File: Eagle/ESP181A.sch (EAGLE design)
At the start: 30 parts

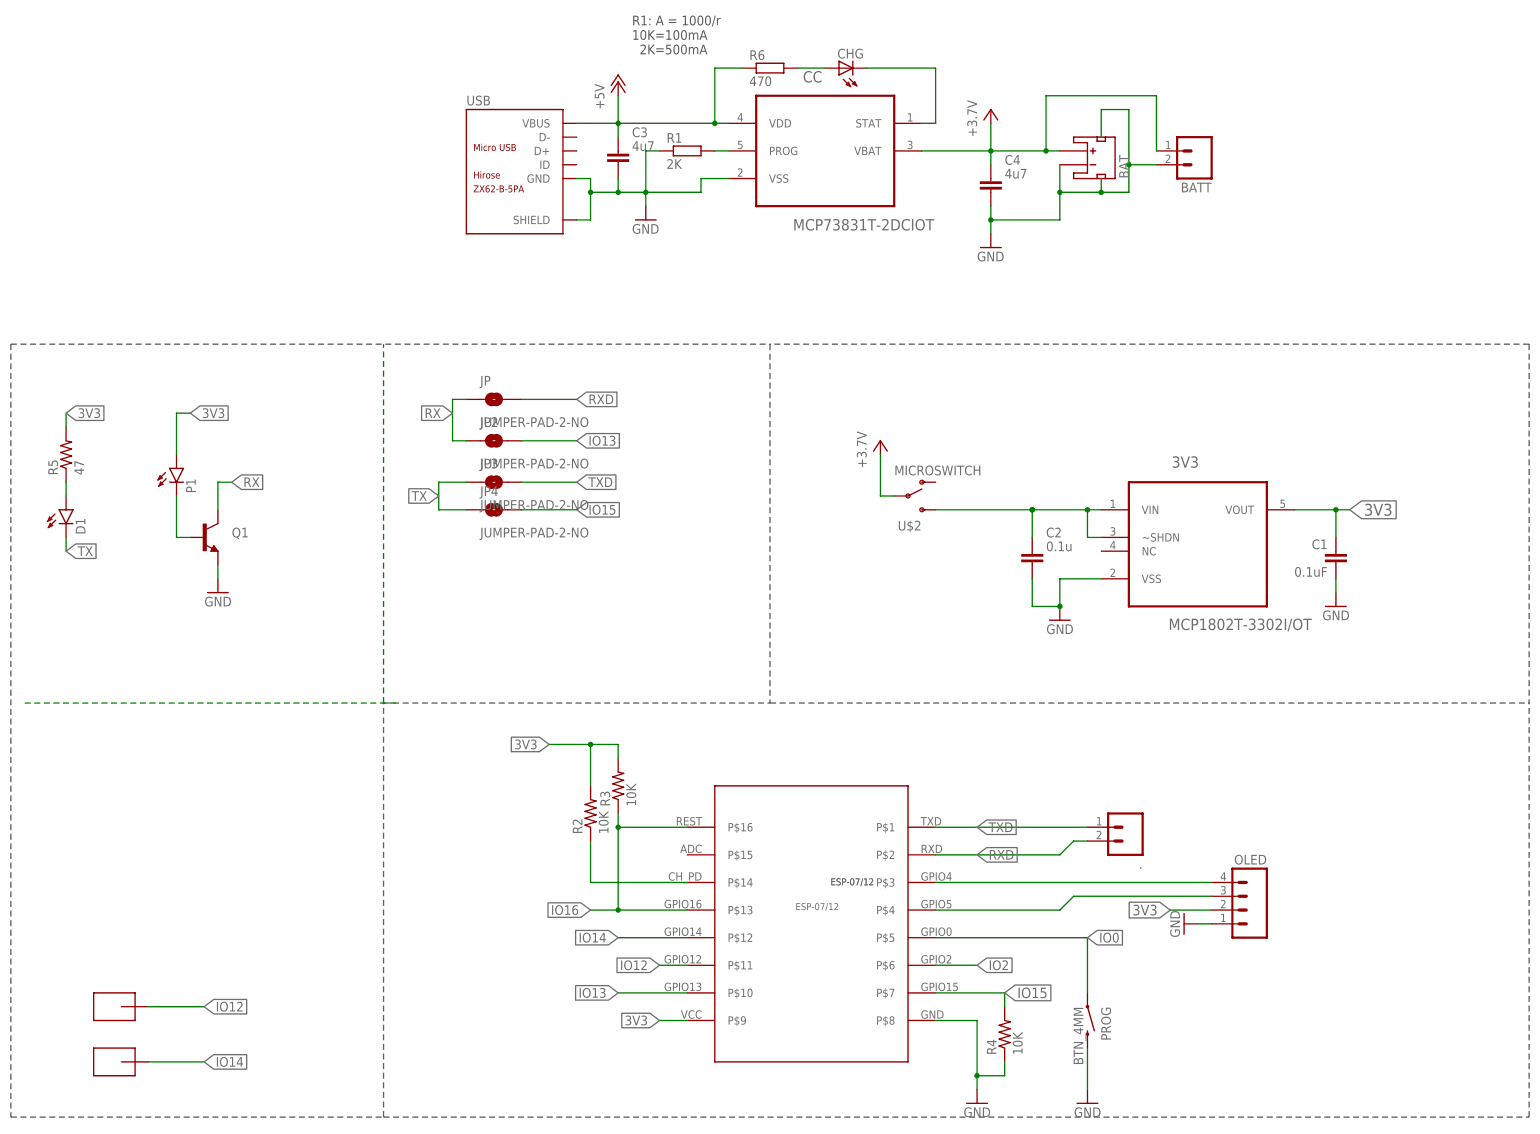
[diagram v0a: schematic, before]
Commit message: Added battery voltage monitor
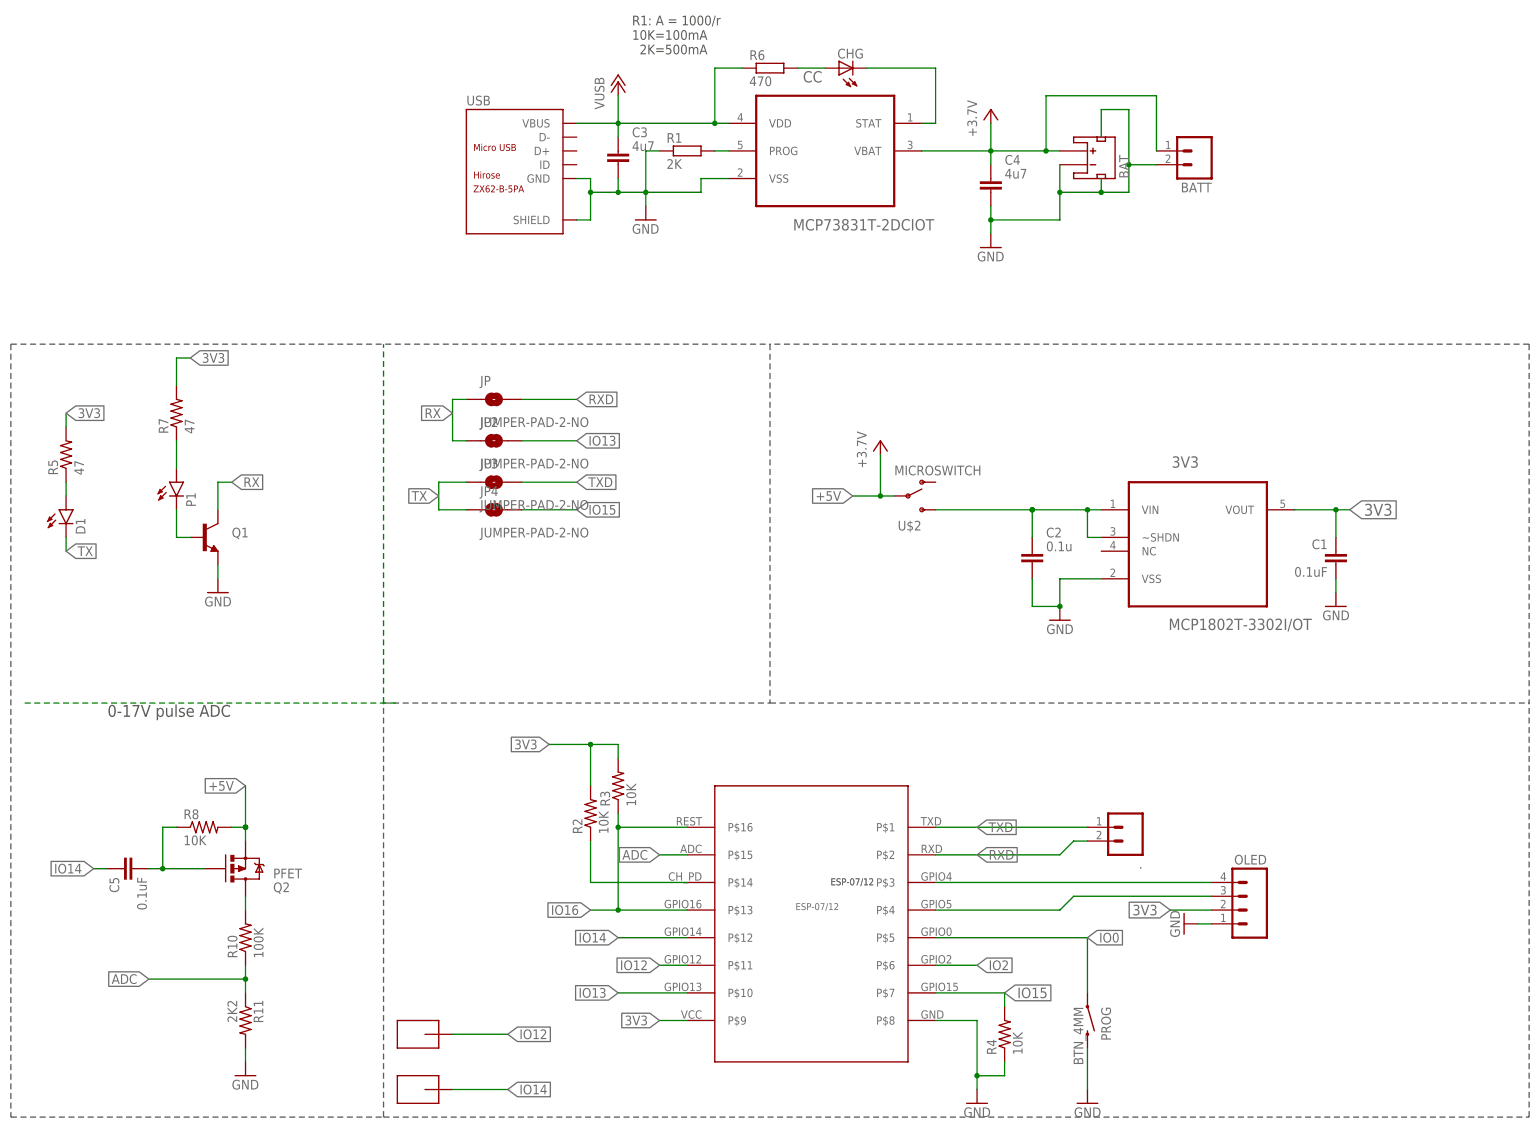
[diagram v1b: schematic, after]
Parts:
- added C5: 0.1uF, SparkFun-Capacitors:CAP
- added Q2: PFET, SparkFun-DiscreteSemi:MOSFET-PCHANNEL
- added R10: 100K, SparkFun-Resistors:RESISTOR0805-RES
- added R11: 2K2, SparkFun-Resistors:RESISTOR0805-RES
- added R7: 47, SparkFun-Resistors:RESISTOR0805-RES
- added R8: 10K, SparkFun-Resistors:RESISTOR0805-RES
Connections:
- new net ADC: R10.1, R11.1, U$1.P$15
- new net N$11: P1.A, R7.1
- new net N$12: C5.2, Q2.G, R8.1
- new net N$13: Q2.D, R10.2
- net +5V: now also Q2.S, R8.2
- net 3V3: now also R7.2; no longer P1.A
- net GND: now also R11.2
- net IO14: now also C5.1
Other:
- note added: "0-17V pulse ADC"
- moved on the sheet: P1
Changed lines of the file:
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@@
 <part name="GND10" library="supply1" deviceset="GND" device=""/>
 <part name="P+2" library="supply1" deviceset="+5V" device="" value="+3.7V"/>
-<part name="P+5" library="supply1" deviceset="+12V" device="" value="+5V"/>
+<part name="VUSB" library="supply1" deviceset="+12V" device="" value="VUSB"/>
 <part name="GND11" library="supply1" deviceset="GND" device=""/>
 <part name="CC" library="Microchip_By_element14_Batch_1" deviceset="MCP73832T-2ACI/OT" device="" value="MCP73831T-2DCIOT"/>
@@
 <part name="U$3" library="CuriousTech" deviceset="SMD-PAD1" device="82X64"/>
 <part name="U$4" library="CuriousTech" deviceset="SMD-PAD1" device="82X64"/>
+<part name="R7" library="SparkFun-Resistors" deviceset="RESISTOR" device="0805-RES" value="47"/>
+<part name="R11" library="SparkFun-Resistors" deviceset="RESISTOR" device="0805-RES" value="2K2"/>
+<part name="GND3" library="supply1" deviceset="GND" device=""/>
+<part name="R10" library="SparkFun-Resistors" deviceset="RESISTOR" device="0805-RES" value="100K"/>
+<part name="Q2" library="SparkFun-DiscreteSemi" deviceset="MOSFET-PCHANNEL" device="" value="PFET"/>
+<part name="C5" library="SparkFun-Capacitors" deviceset="CAP" device="" value="0.1uF"/>
+<part name="R8" library="SparkFun-Resistors" deviceset="RESISTOR" device="0805-RES" value="10K"/>
 </parts>
 <sheets>
@@
 10K=100mA
   2K=500mA</text>
+<text x="17.78" y="73.66" size="2.1844" layer="97">0-17V pulse ADC</text>
 </plain>
 <instances>
@@
 <instance part="GND10" gate="1" x="116.84" y="165.1"/>
 <instance part="P+2" gate="1" x="180.34" y="185.42"/>
-<instance part="P+5" gate="1" x="111.76" y="190.5"/>
+<instance part="VUSB" gate="1" x="111.76" y="190.5"/>
 <instance part="GND11" gate="1" x="180.34" y="160.02"/>
 <instance part="CC" gate="A" x="149.86" y="180.34"/>
@@
 <instance part="R6" gate="G$1" x="139.7" y="193.04"/>
 <instance part="BAT" gate="G$1" x="198.12" y="177.8" rot="MR90"/>
-<instance part="P1" gate="G$1" x="30.48" y="119.38"/>
+<instance part="P1" gate="G$1" x="30.48" y="116.84"/>
 <instance part="D1" gate="G$1" x="10.16" y="111.76"/>
 <instance part="R5" gate="G$1" x="10.16" y="121.92" rot="R90"/>
@@
 <instance part="C2" gate="C" x="187.96" y="101.6"/>
 <instance part="U$2" gate="G$1" x="167.64" y="114.3"/>
-<instance part="U$3" gate="G$1" x="20.32" y="10.16" rot="R180"/>
-<instance part="U$4" gate="G$1" x="20.32" y="20.32" rot="R180"/>
+<instance part="U$3" gate="G$1" x="76.2" y="5.08" rot="R180"/>
+<instance part="U$4" gate="G$1" x="76.2" y="15.24" rot="R180"/>
+<instance part="R7" gate="G$1" x="30.48" y="129.54" rot="R90"/>
+<instance part="R11" gate="G$1" x="43.18" y="17.78" rot="R270"/>
+<instance part="GND3" gate="1" x="43.18" y="7.62"/>
+<instance part="R10" gate="G$1" x="43.18" y="33.02" rot="R90"/>
+<instance part="Q2" gate="G$1" x="43.18" y="45.72" rot="MR180"/>
+<instance part="C5" gate="G$1" x="22.86" y="45.72" rot="MR270"/>
+<instance part="R8" gate="G$1" x="35.56" y="53.34"/>
 </instances>
 <busses>
@@
 </segment>
 <segment>
-<label x="33.02" y="129.54" size="1.778" layer="95" xref="yes"/>
-<pinref part="P1" gate="G$1" pin="A"/>
-<wire x1="30.48" y1="121.92" x2="30.48" y2="129.54" width="0.1524" layer="91"/>
-<wire x1="30.48" y1="129.54" x2="33.02" y2="129.54" width="0.1524" layer="91"/>
+<label x="33.02" y="139.7" size="1.778" layer="95" xref="yes"/>
+<wire x1="30.48" y1="139.7" x2="33.02" y2="139.7" width="0.1524" layer="91"/>
+<pinref part="R7" gate="G$1" pin="2"/>
+<wire x1="30.48" y1="134.62" x2="30.48" y2="139.7" width="0.1524" layer="91"/>
 </segment>
 </net>
@@
 <wire x1="38.1" y1="101.6" x2="38.1" y2="99.06" width="0.1524" layer="91"/>
 </segment>
+<segment>
+<pinref part="GND3" gate="1" pin="GND"/>
+<pinref part="R11" gate="G$1" pin="2"/>
+<wire x1="43.18" y1="10.16" x2="43.18" y2="12.7" width="0.1524" layer="91"/>
+</segment>
 </net>
 <net name="TXD" class="0">
@@
 <segment>
 <pinref part="U$4" gate="G$1" pin="P$1"/>
-<wire x1="25.4" y1="20.32" x2="35.56" y2="20.32" width="0.1524" layer="91"/>
-<label x="35.56" y="20.32" size="1.778" layer="95" xref="yes"/>
+<wire x1="81.28" y1="15.24" x2="91.44" y2="15.24" width="0.1524" layer="91"/>
+<label x="91.44" y="15.24" size="1.778" layer="95" xref="yes"/>
 </segment>
 </net>
@@
 <segment>
 <pinref part="U$3" gate="G$1" pin="P$1"/>
-<wire x1="25.4" y1="10.16" x2="35.56" y2="10.16" width="0.1524" layer="91"/>
-<label x="35.56" y="10.16" size="1.778" layer="95" xref="yes"/>
+<wire x1="81.28" y1="5.08" x2="91.44" y2="5.08" width="0.1524" layer="91"/>
+<label x="91.44" y="5.08" size="1.778" layer="95" xref="yes"/>
+</segment>
+<segment>
+<pinref part="C5" gate="G$1" pin="1"/>
+<wire x1="17.78" y1="45.72" x2="15.24" y2="45.72" width="0.1524" layer="91"/>
+<label x="15.24" y="45.72" size="1.778" layer="95" rot="R180" xref="yes"/>
 </segment>
 </net>
@@
 <pinref part="P+1" gate="1" pin="+5V"/>
 <pinref part="U$2" gate="G$1" pin="P"/>
+<wire x1="160.02" y1="114.3" x2="154.94" y2="114.3" width="0.1524" layer="91"/>
+<junction x="160.02" y="114.3"/>
+<label x="154.94" y="114.3" size="1.778" layer="95" rot="R180" xref="yes"/>
+</segment>
+<segment>
+<label x="43.18" y="60.96" size="1.778" layer="95" rot="R180" xref="yes"/>
+<pinref part="Q2" gate="G$1" pin="S"/>
+<wire x1="43.18" y1="50.8" x2="43.18" y2="53.34" width="0.1524" layer="91"/>
+<pinref part="R8" gate="G$1" pin="2"/>
+<wire x1="40.64" y1="53.34" x2="43.18" y2="53.34" width="0.1524" layer="91"/>
+<junction x="43.18" y="53.34"/>
+<junction x="43.18" y="53.34"/>
+<wire x1="43.18" y1="60.96" x2="43.18" y2="53.34" width="0.1524" layer="91"/>
 </segment>
 </net>
@@
 <net name="VBUS" class="0">
 <segment>
-<pinref part="P+5" gate="1" pin="+12V"/>
+<pinref part="VUSB" gate="1" pin="+12V"/>
 <wire x1="111.76" y1="187.96" x2="111.76" y2="182.88" width="0.1524" layer="91"/>
 <wire x1="111.76" y1="180.34" x2="111.76" y2="182.88" width="0.1524" layer="91"/>
@@
 <wire x1="33.02" y1="106.68" x2="30.48" y2="106.68" width="0.1524" layer="91"/>
 <pinref part="P1" gate="G$1" pin="C"/>
-<wire x1="30.48" y1="106.68" x2="30.48" y2="114.3" width="0.1524" layer="91"/>
-</segment>
-</net>
+<wire x1="30.48" y1="106.68" x2="30.48" y2="111.76" width="0.1524" layer="91"/>
+</segment>
+</net>
+<net name="N$11" class="0">
+<segment>
+<pinref part="R7" gate="G$1" pin="1"/>
+<pinref part="P1" gate="G$1" pin="A"/>
+<wire x1="30.48" y1="124.46" x2="30.48" y2="119.38" width="0.1524" layer="91"/>
+</segment>
+</net>
+<net name="ADC" class="0">
+<segment>
+<label x="25.4" y="25.4" size="1.778" layer="95" rot="R180" xref="yes"/>
+<pinref part="R11" gate="G$1" pin="1"/>
+<wire x1="43.18" y1="25.4" x2="25.4" y2="25.4" width="0.1524" layer="91"/>
+<wire x1="43.18" y1="22.86" x2="43.18" y2="25.4" width="0.1524" layer="91"/>
+<junction x="43.18" y="25.4"/>
+<pinref part="R10" gate="G$1" pin="1"/>
+<wire x1="43.18" y1="25.4" x2="43.18" y2="27.94" width="0.1524" layer="91"/>
+</segment>
+<segment>
+<pinref part="U$1" gate="G$1" pin="P$15"/>
+<wire x1="124.46" y1="48.26" x2="119.38" y2="48.26" width="0.1524" layer="91"/>
+<label x="119.38" y="48.26" size="1.778" layer="95" rot="R180" xref="yes"/>
+</segment>
+</net>
+<net name="N$12" class="0">
+<segment>
+<pinref part="C5" gate="G$1" pin="2"/>
+<pinref part="Q2" gate="G$1" pin="G"/>
+<wire x1="25.4" y1="45.72" x2="27.94" y2="45.72" width="0.1524" layer="91"/>
+<pinref part="R8" gate="G$1" pin="1"/>
+<wire x1="27.94" y1="45.72" x2="35.56" y2="45.72" width="0.1524" layer="91"/>
+<wire x1="30.48" y1="53.34" x2="27.94" y2="53.34" width="0.1524" layer="91"/>
+<wire x1="27.94" y1="53.34" x2="27.94" y2="45.72" width="0.1524" layer="91"/>
+<junction x="27.94" y="45.72"/>
+</segment>
+</net>
+<net name="N$13" class="0">
+<segment>
+<pinref part="R10" gate="G$1" pin="2"/>
+<pinref part="Q2" gate="G$1" pin="D"/>
+<wire x1="43.18" y1="38.1" x2="43.18" y2="40.64" width="0.1524" layer="91"/>
+</segment>
+</net>
